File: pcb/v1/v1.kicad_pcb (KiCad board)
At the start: 2 copper layers, 110 parts, among them J1 USB_C_Receptacle_USB2.0_16P, SW1 SW_Push, SW2 SW_Push, U1 NCP1117-3.3_SOT223, U2 USB6B1, U3 W25Q128JVS, U4 RP2040, X1 ABM8-272-T3

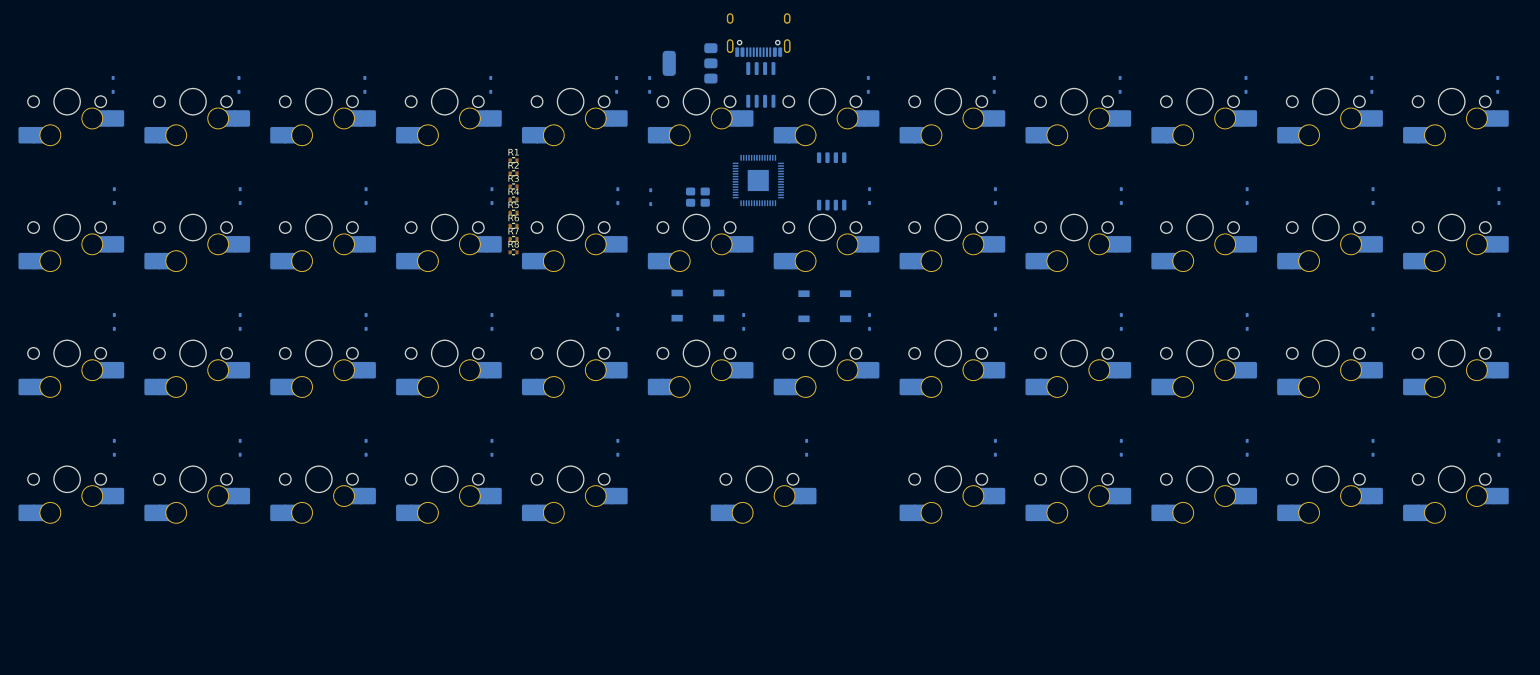
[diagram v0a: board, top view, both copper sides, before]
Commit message: centering pcb
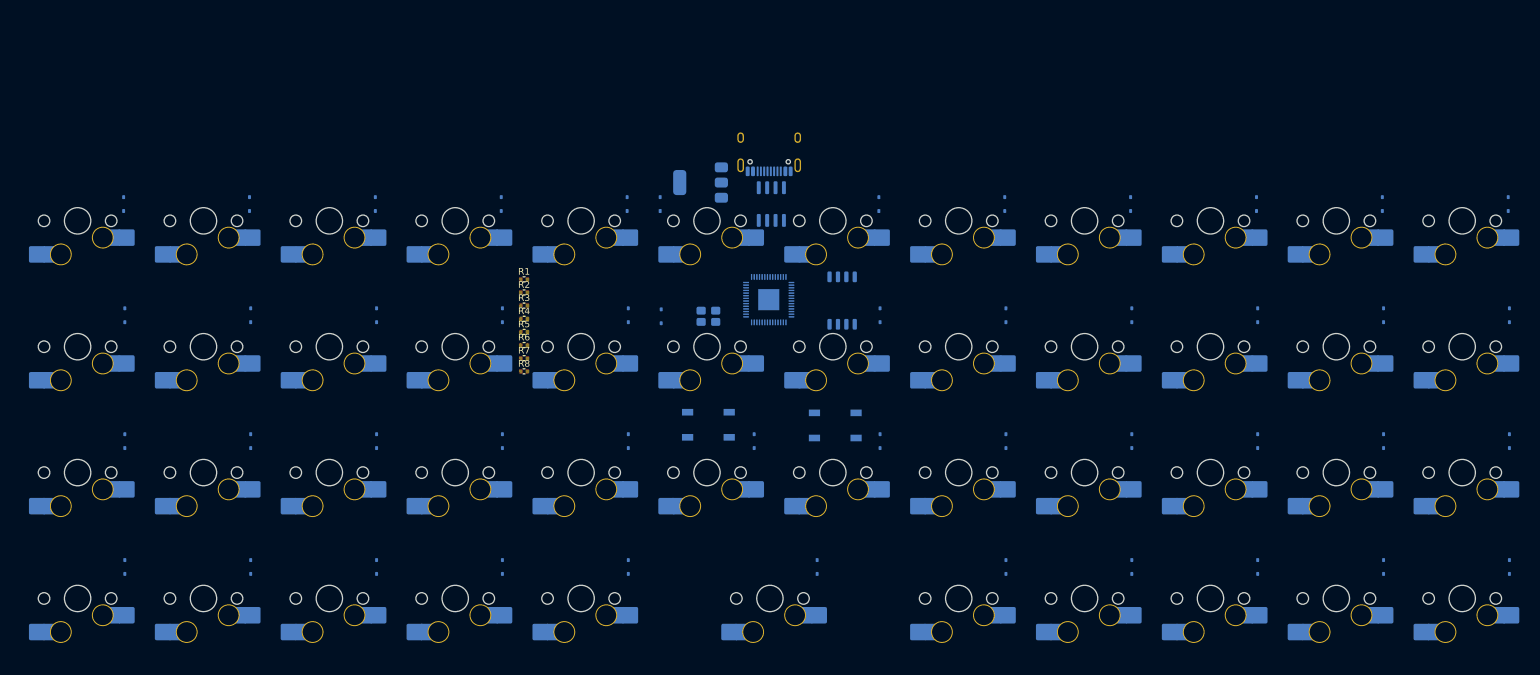
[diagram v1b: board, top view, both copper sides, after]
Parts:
- moved R5 18.1 mm to (113.0, 85.9)
- moved R8 18.1 mm to (113.0, 91.9)
- moved MX1 18.1 mm to (45.4, 69.1)
- moved MX11 18.1 mm to (235.9, 69.1)
- moved MX12 18.1 mm to (255.0, 69.1)
- moved MX2 18.1 mm to (64.5, 69.1)
- moved MX3 18.1 mm to (83.5, 69.1)
- moved MX4 18.1 mm to (102.6, 69.1)
- moved MX5 18.1 mm to (121.6, 69.1)
- moved MX6 18.1 mm to (140.7, 69.1)
- moved MX7 18.1 mm to (159.7, 69.1)
- moved MX8 18.1 mm to (178.8, 69.1)
- moved MX9 18.1 mm to (197.8, 69.1)
- moved R3 18.1 mm to (113.0, 81.9)
- moved U3 18.1 mm to (161.1, 81.1)
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
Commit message: bottom case rev 1 and pcb updates
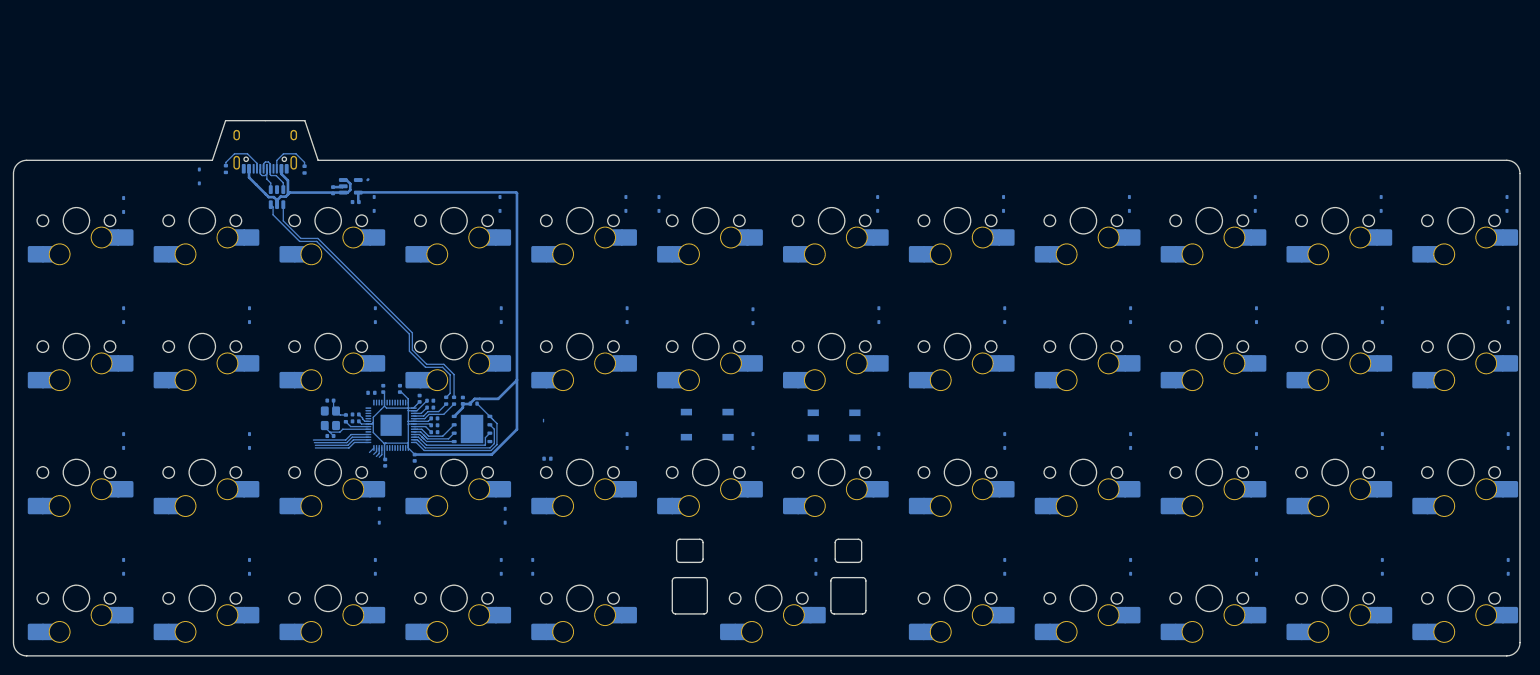
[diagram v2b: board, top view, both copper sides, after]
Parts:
- removed U2: USB6B1, Package_SO:SOIC-8_3.9x4.9mm_P1.27mm
- added C1: 100n, Capacitor_SMD:C_0402_1005Metric, B.Cu at (103.7, 96.3)
- added C10: 1u, Capacitor_SMD:C_0402_1005Metric, B.Cu at (87.5, 98.4)
- added C11: 100n, Capacitor_SMD:C_0402_1005Metric, B.Cu at (99.4, 101.1)
- added C12: 100n, Capacitor_SMD:C_0402_1005Metric, B.Cu at (98.8, 97.3)
- added C13: 1u, Capacitor_SMD:C_0402_1005Metric, B.Cu at (98.8, 96.3)
- added C14: 100n, Capacitor_SMD:C_0402_1005Metric, B.Cu at (97.2, 96.0)
- added C15: 100n, Capacitor_SMD:C_0402_1005Metric, B.Cu at (94.2, 94.5)
- added C16: 100n, Capacitor_SMD:C_0402_1005Metric, B.Cu at (99.4, 100.0)
- added C17: 100n, Capacitor_SMD:C_0402_1005Metric, B.Cu at (99.4, 99.0)
- added C2: 1u, Capacitor_SMD:C_0402_1005Metric, B.Cu at (84.1, 64.4)
- added C3: 1u, Capacitor_SMD:C_0402_1005Metric, B.Cu at (87.5, 66.2)
- added C4: 15p, Capacitor_SMD:C_0402_1005Metric, B.Cu at (83.7, 101.6)
- added C5: 15p, Capacitor_SMD:C_0402_1005Metric, B.Cu at (83.7, 96.3)
- added C6: 100n, Capacitor_SMD:C_0402_1005Metric, B.Cu at (87.5, 99.4)
- added C7: 100n, Capacitor_SMD:C_0402_1005Metric, B.Cu at (91.7, 94.5)
- added C8: 100n, Capacitor_SMD:C_0402_1005Metric, B.Cu at (92.0, 105.7)
- added C9: 100n, Capacitor_SMD:C_0402_1005Metric, B.Cu at (96.4, 104.9)
- added S1: choc_stab, PCM_marbastlib-xp-choc:STAB_choc_2u, F.Cu at (150.1, 126.3)
- added U5: AP2112K-3.3, Package_TO_SOT_SMD:SOT-23-5, B.Cu at (86.8, 63.8)
- R1, R2, R3, R4, R5, R6, R7, R8: moved to B.Cu
- U1: value NCP1117-3.3_SOT223 -> USBLC6-2SC6; footprint Package_TO_SOT_SMD:SOT-223-3_TabPin2 -> Package_TO_SOT_SMD:SOT-23-6
- U3: footprint Package_SO:SOIC-8_5.3x5.3mm_P1.27mm -> Package_SON:WSON-8-1EP_6x5mm_P1.27mm_EP3.4x4.3mm
- moved J1 76.3 mm to (73.8, 57.2)
- moved U1 64.1 mm to (75.6, 65.5), turned to -90 degrees
- moved U4 60.2 mm to (92.9, 100.0)
- moved U3 59.3 mm to (105.1, 100.6), turned to 180 degrees
- moved X1 59.3 mm to (83.7, 99.0), turned to 90 degrees
- moved R1 48.1 mm to (67.9, 61.2), turned to -90 degrees
- moved R2 38.1 mm to (79.8, 61.3), turned to -90 degrees
- moved R5 30.0 mm to (86.0, 99.0), turned to -90 degrees
- moved R6 24.2 mm to (89.9, 95.1), turned to 180 degrees
- moved R4 21.5 mm to (116.5, 105.1), turned to 180 degrees
- moved R3 16.7 mm to (105.4, 96.7)
- moved D41 14.5 mm to (114.3, 121.4)
- moved D18 13.9 mm to (147.6, 83.5)
- moved R7 13.4 mm to (101.2, 96.3), turned to -90 degrees
- moved R8 11.5 mm to (102.4, 96.3), turned to -90 degrees
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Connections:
- net Net-(U4-USB_DM) renamed /RPD+
- net Net-(U4-USB_DP) renamed /RPD-
- U1 pad 1: GND -> Net-(J1-D--PadA7)
- U1 pad 2: +3V3 -> GND
- U1 pad 3: VBUS -> Net-(J1-D+-PadA6)
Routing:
- net +3V3: track 0.00 -> 136.8 mm
- net DATA-: track 0.00 -> 43.7 mm
- net DATA+: track 0.00 -> 42.9 mm
- net VBUS: track 0.00 -> 26.7 mm
- net QSPI_SS: track 0.00 -> 21.5 mm
- net QSPI_SD1: track 0.00 -> 16.4 mm
- net QSPI_SD2: track 0.00 -> 13.5 mm
- net COL12: track 0.00 -> 8.66 mm
- net XIN: track 0.00 -> 8.52 mm
- net COL11: track 0.00 -> 8.52 mm
- net COL9: track 0.00 -> 8.37 mm
- net COL10: track 0.00 -> 8.37 mm
- net QSPI_SCLK: track 0.00 -> 7.52 mm
- net +1V1: track 0.00 -> 7.29 mm
- net QSPI_SD3: track 0.00 -> 7.26 mm
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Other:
- board outline added: 228 x 81 mm

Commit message: pcb v1
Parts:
- moved SW2 65.6 mm to (75.2, 99.0)
- moved SW1 44.7 mm to (115.2, 99.3)
- moved D2 16.1 mm to (72.0, 76.2), turned to 90 degrees
- moved D41 14.9 mm to (129.2, 121.4)
- moved D6 14.9 mm to (148.3, 66.1)
- moved R4 11.8 mm to (107.5, 97.4)
- moved D36 11.3 mm to (262.5, 113.7), turned to 90 degrees
- moved D35 11.3 mm to (243.5, 113.7), turned to 90 degrees
- moved D34 11.3 mm to (224.4, 113.7), turned to 90 degrees
- moved D33 11.3 mm to (205.4, 113.7), turned to 90 degrees
- moved D32 11.3 mm to (186.3, 113.7), turned to 90 degrees
- moved D31 11.3 mm to (167.3, 113.7), turned to 90 degrees
- moved D30 11.3 mm to (148.2, 113.7), turned to 90 degrees
- moved D29 11.3 mm to (129.2, 113.7), turned to 90 degrees
- moved D26 11.3 mm to (72.0, 113.7), turned to 90 degrees
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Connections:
- U4 pad 11: COL5 -> unconnected-(U4-GPIO8-Pad11)
- U4 pad 12: COL6 -> unconnected-(U4-GPIO9-Pad12)
- U4 pad 13: COL7 -> unconnected-(U4-GPIO10-Pad13)
- U4 pad 14: COL8 -> unconnected-(U4-GPIO11-Pad14)
- U4 pad 15: COL9 -> ROW4
- U4 pad 16: COL10 -> ROW3
- U4 pad 17: COL11 -> COL1
- U4 pad 18: COL12 -> COL2
- U4 pad 2: ROW1 -> COL5
- U4 pad 29: unconnected-(U4-GPIO18-Pad29) -> COL3
- U4 pad 3: ROW2 -> COL12
- U4 pad 30: unconnected-(U4-GPIO19-Pad30) -> ROW1
- U4 pad 31: unconnected-(U4-GPIO20-Pad31) -> ROW2
- U4 pad 35: unconnected-(U4-GPIO23-Pad35) -> COL6
- U4 pad 36: unconnected-(U4-GPIO24-Pad36) -> COL7
- U4 pad 38: unconnected-(U4-GPIO26/ADC0-Pad38) -> COL4
- U4 pad 4: ROW3 -> COL11
- U4 pad 5: ROW4 -> COL10
- U4 pad 6: COL1 -> COL8
- U4 pad 7: COL2 -> COL9
- U4 pad 8: COL3 -> unconnected-(U4-GPIO6-Pad8)
- U4 pad 9: COL4 -> unconnected-(U4-GPIO7-Pad9)
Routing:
- net ROW1: track 0.00 -> 246.0 mm, vias 0 -> 3
- net ROW4: track 0.00 -> 242.3 mm, vias 0 -> 2
- net ROW2: track 0.00 -> 239.1 mm, vias 0 -> 2
- net ROW3: track 0.00 -> 234.6 mm
- net COL12: track 8.66 -> 224.3 mm, vias 0 -> 3
- net COL11: track 8.52 -> 206.4 mm, vias 0 -> 3
- net COL10: track 8.37 -> 188.5 mm, vias 0 -> 3
- net COL9: track 8.37 -> 175.7 mm, vias 0 -> 3
- net COL8: track 0.95 -> 153.5 mm, vias 0 -> 3
- net COL6: track 1.46 -> 121.0 mm, vias 0 -> 2
- net COL7: track 1.15 -> 116.0 mm, vias 0 -> 2
- net COL1: track 0.00 -> 108.4 mm
- net COL2: track 0.00 -> 92.7 mm
- net COL5: track 1.56 -> 83.4 mm
- net COL3: track 0.00 -> 68.4 mm
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- added copper zone on B.Cu, net +1V1
- added copper zone on B.Cu, net +3V3
- added copper zone on B.Cu, net GND
- added copper zone on F.Cu, net GND

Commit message: pcb v1
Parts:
- added H1: M2, MountingHole:MountingHole_2.2mm_M2_Pad, F.Cu at (45.2, 78.6)
- added H2: M2, MountingHole:MountingHole_2.2mm_M2_Pad, F.Cu at (64.3, 97.6)
- added H3: M2, MountingHole:MountingHole_2.2mm_M2_Pad, F.Cu at (45.2, 116.7)
- added H4: M2, MountingHole:MountingHole_2.2mm_M2_Pad, F.Cu at (150.0, 115.0)
- added H5: M2, MountingHole:MountingHole_2.2mm_M2_Pad, F.Cu at (254.8, 78.6)
- added H6: M2, MountingHole:MountingHole_2.2mm_M2_Pad, F.Cu at (235.7, 97.6)
- added H7: M2, MountingHole:MountingHole_2.2mm_M2_Pad, F.Cu at (254.8, 116.7)
- added H8: M2, MountingHole:MountingHole_2.2mm_M2_Pad, F.Cu at (150.0, 78.6)
- moved D36 10.1 mm to (262.5, 103.6), turned to -90 degrees
- moved D30 8.93 mm to (148.2, 104.8), turned to -90 degrees
- moved D15 2.08 mm to (91.1, 84.2)
- moved C1 1.46 mm to (102.4, 97.6), turned to 180 degrees
- moved R4 1.31 mm to (106.3, 97.6)
- moved U3 1.03 mm to (104.0, 101.2)
- moved R3 1.02 mm to (104.3, 97.6)
- moved D16 0.60 mm to (110.1, 82.7)
- moved D17 0.60 mm to (129.2, 82.7)
- moved D18 0.60 mm to (148.2, 82.9)
- moved D19 0.60 mm to (167.3, 82.7)
- moved D20 0.60 mm to (186.3, 82.7)
- moved D21 0.60 mm to (205.4, 82.7)
- moved D22 0.60 mm to (224.4, 82.7)
- moved D23 0.60 mm to (243.5, 82.7)
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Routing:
- net ROW3: track 234.6 -> 251.1 mm
- net COL4: track 64.0 -> 78.1 mm
- net COL8: track 153.5 -> 159.9 mm
- net GND: track 52.5 -> 46.7 mm, vias 53 -> 63
- net COL10: track 188.5 -> 194.0 mm
- net ROW2: track 239.1 -> 233.6 mm
- net COL11: track 206.4 -> 211.7 mm
- net COL12: track 224.3 -> 229.4 mm
- net COL9: track 175.7 -> 179.4 mm
- net Net-(D36-A): track 3.12 -> 5.76 mm
- net COL2: track 92.7 -> 95.0 mm
- net QSPI_SCLK: track 7.52 -> 5.88 mm
- net /BOOT: track 10.3 -> 11.9 mm
- net Net-(D15-A): track 7.60 -> 6.05 mm
- net QSPI_SD0: track 7.01 -> 5.53 mm
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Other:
- board size 228 x 81 mm -> 228.6 x 80.7 mm
- board text added: "BOOT"
- board text added: "RESET"

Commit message: Minor placement changes and mates
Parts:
- moved J1 0.93 mm to (73.8, 58.1)
- moved R1 0.93 mm to (67.9, 62.2)
- moved R2 0.93 mm to (79.8, 62.2)
- moved U1 0.93 mm to (75.6, 66.4)
- moved C2 0.89 mm to (84.1, 65.3)
- moved C3 0.89 mm to (87.5, 67.1)
- moved U5 0.89 mm to (86.8, 64.7)
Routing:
- net VBUS: track 30.3 -> 32.3 mm
- net DATA-: track 50.1 -> 49.1 mm
- net DATA+: track 51.2 -> 50.3 mm

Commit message: pcb BOM updates
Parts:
- U3: value W25Q128JVS -> W25Q128JVP
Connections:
- U4 pad 15: ROW4 -> unconnected-(U4-GPIO12-Pad15)
- U4 pad 8: unconnected-(U4-GPIO6-Pad8) -> ROW4
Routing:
- net ROW4: track 242.2 -> 230.8 mm, vias 2 -> 0
- net COL12: track 229.4 -> 230.7 mm, vias 3 -> 1
- net COL11: track 211.7 -> 212.7 mm, vias 3 -> 1
- net COL9: track 179.4 -> 178.8 mm, vias 3 -> 1
- net COL10: track 194.0 -> 194.4 mm, vias 3 -> 1
- net COL8: vias 3 -> 1
- net ROW3: vias 0 -> 2
- net GND: vias 63 -> 67

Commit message: pcb updates
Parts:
- moved D30 2.53 mm to (148.2, 102.2)
- moved H4 0.79 mm to (150.0, 115.8)
- moved C8 0.37 mm to (91.8, 105.8)
- moved C15 0.21 mm to (94.5, 95.4)
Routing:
- net ROW3: track 251.1 -> 260.6 mm
- net COL4: track 78.1 -> 85.7 mm
- net +3V3: track 144.4 -> 137.7 mm
- net COL11: track 212.7 -> 219.3 mm
- net COL2: track 95.0 -> 98.5 mm
- net COL7: track 116.0 -> 112.6 mm
- net VBUS: track 32.3 -> 28.9 mm
- net GND: track 46.7 -> 49.8 mm, vias 67 -> 79
- net COL12: track 230.7 -> 227.9 mm, vias 1 -> 0
- net COL10: track 194.4 -> 197.1 mm
- net Net-(D30-A): track 4.03 -> 6.56 mm
- net COL8: track 159.9 -> 162.4 mm
- net ROW2: track 233.6 -> 235.6 mm
- net COL6: track 121.0 -> 119.2 mm
- net COL9: track 178.8 -> 180.0 mm
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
